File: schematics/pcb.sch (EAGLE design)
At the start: 14 parts

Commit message: Further work on pcb schematics
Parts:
- added C5: 0.33uF, rcl:C-EUC0805
- added C6: 0.1uF, rcl:C-EUC0805
- added CONFIRM, LEFT, RIGHT: CHERRY_MX_LED, cherry:CHERRY_MX_LED
- added IC1: 7805TV, linear:7805TV
- added R6, R7, R8: 1k, rcl:R-EU_R0805
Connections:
- new net N$15: RIGHTG$1.2, UIM.PD6(AIN0/OC0A/PCINT22)
- new net N$16: CONFIRMG$1.2, UIM.PD7(AIN1/PCINT23)
- new net N$18: LEFTLED.A, R6.2
- new net N$19: R7.2, RIGHTLED.A
- new net N$20: CONFIRMLED.A, R8.2
- new net N$9: LEFTG$1.2, UIM.PD5(T1/OC0B/PCINT21)
- new net PWRIN: C5.1, IC1.VI
- net +5V: now also C6.1, IC1.VO, R6.1, R7.1, R8.1
- net GND: now also C5.2, C6.2, CONFIRMG$1.1, CONFIRMLED.C, IC1.GND, LEFTG$1.1, LEFTLED.C, RIGHTG$1.1, RIGHTLED.C
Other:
- moved on the sheet: C3, C4, Q2, R5, TARGET_ISP, UIM

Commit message: Further work on pcb schematics
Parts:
- added BAT: 9V, con-wago-500:W237-102
- added C7, C8: 100nF, rcl:C-EUC0805
- added S1: (no value), Wurth_Switch_WS-SLTV:452404020202
- added U$1: 128X64-I2C-OLED, Parts:128X64-I2C-OLED
- Q1, Q2: value (none) -> 16Mhz
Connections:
- new net N$17: BAT-1.KL, S1.COM1
- new net N$21: C7.1, UIM.AREF
- new net N$22: C8.1, PROGRAMMER.AREF
- net +5V: now also PROGRAMMER.AVCC, U$1.VCC, UIM.AVCC
- net GND: now also BAT-2.KL, C7.2, C8.2, PROGRAMMER.AGND, U$1.GND, UIM.AGND
- net N$1: now also U$1.SCL
- net N$2: now also U$1.SDA
- net PWRIN: now also S1.4
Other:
- note added: "I2C-OLED"
- moved on the sheet: R1, R2, R3

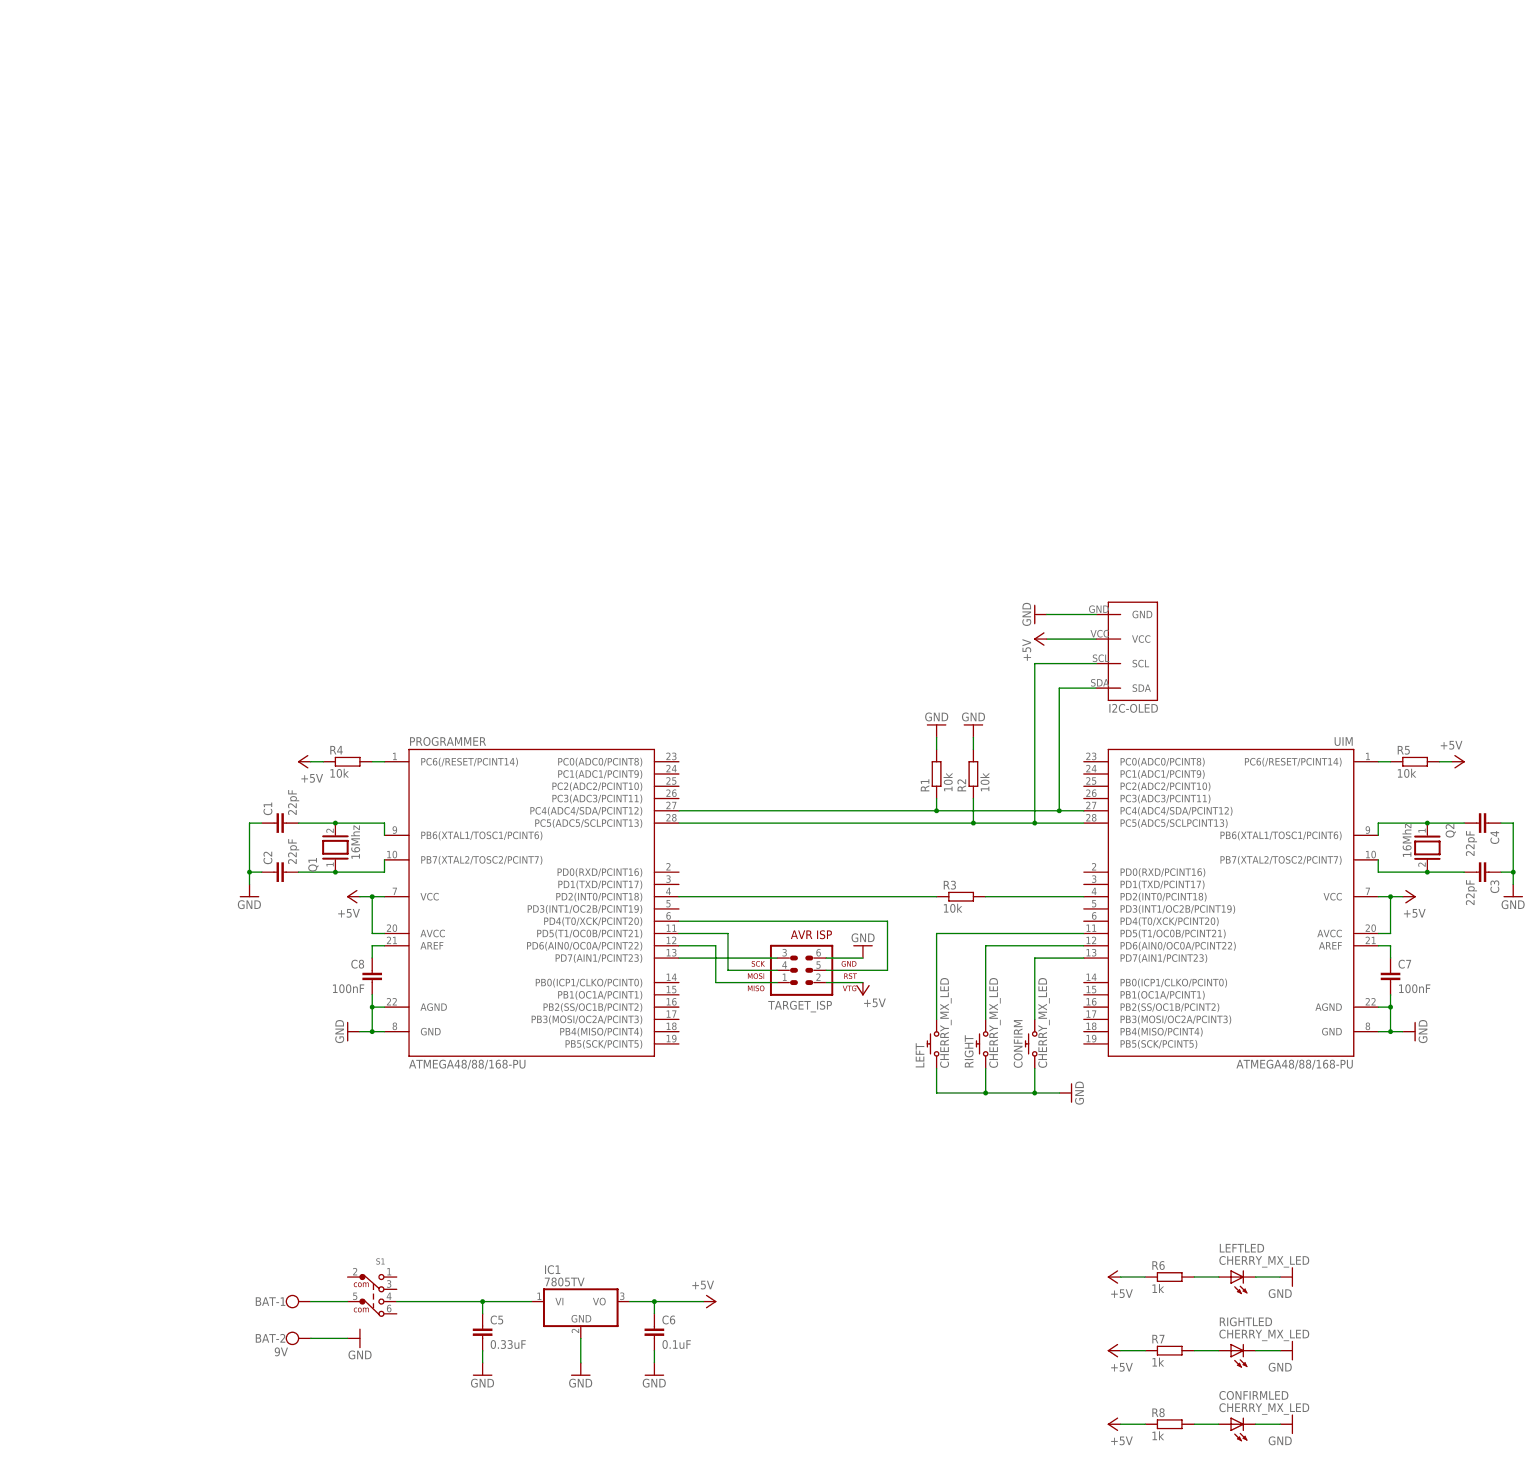
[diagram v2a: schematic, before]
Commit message: Added SD-Card to PCB
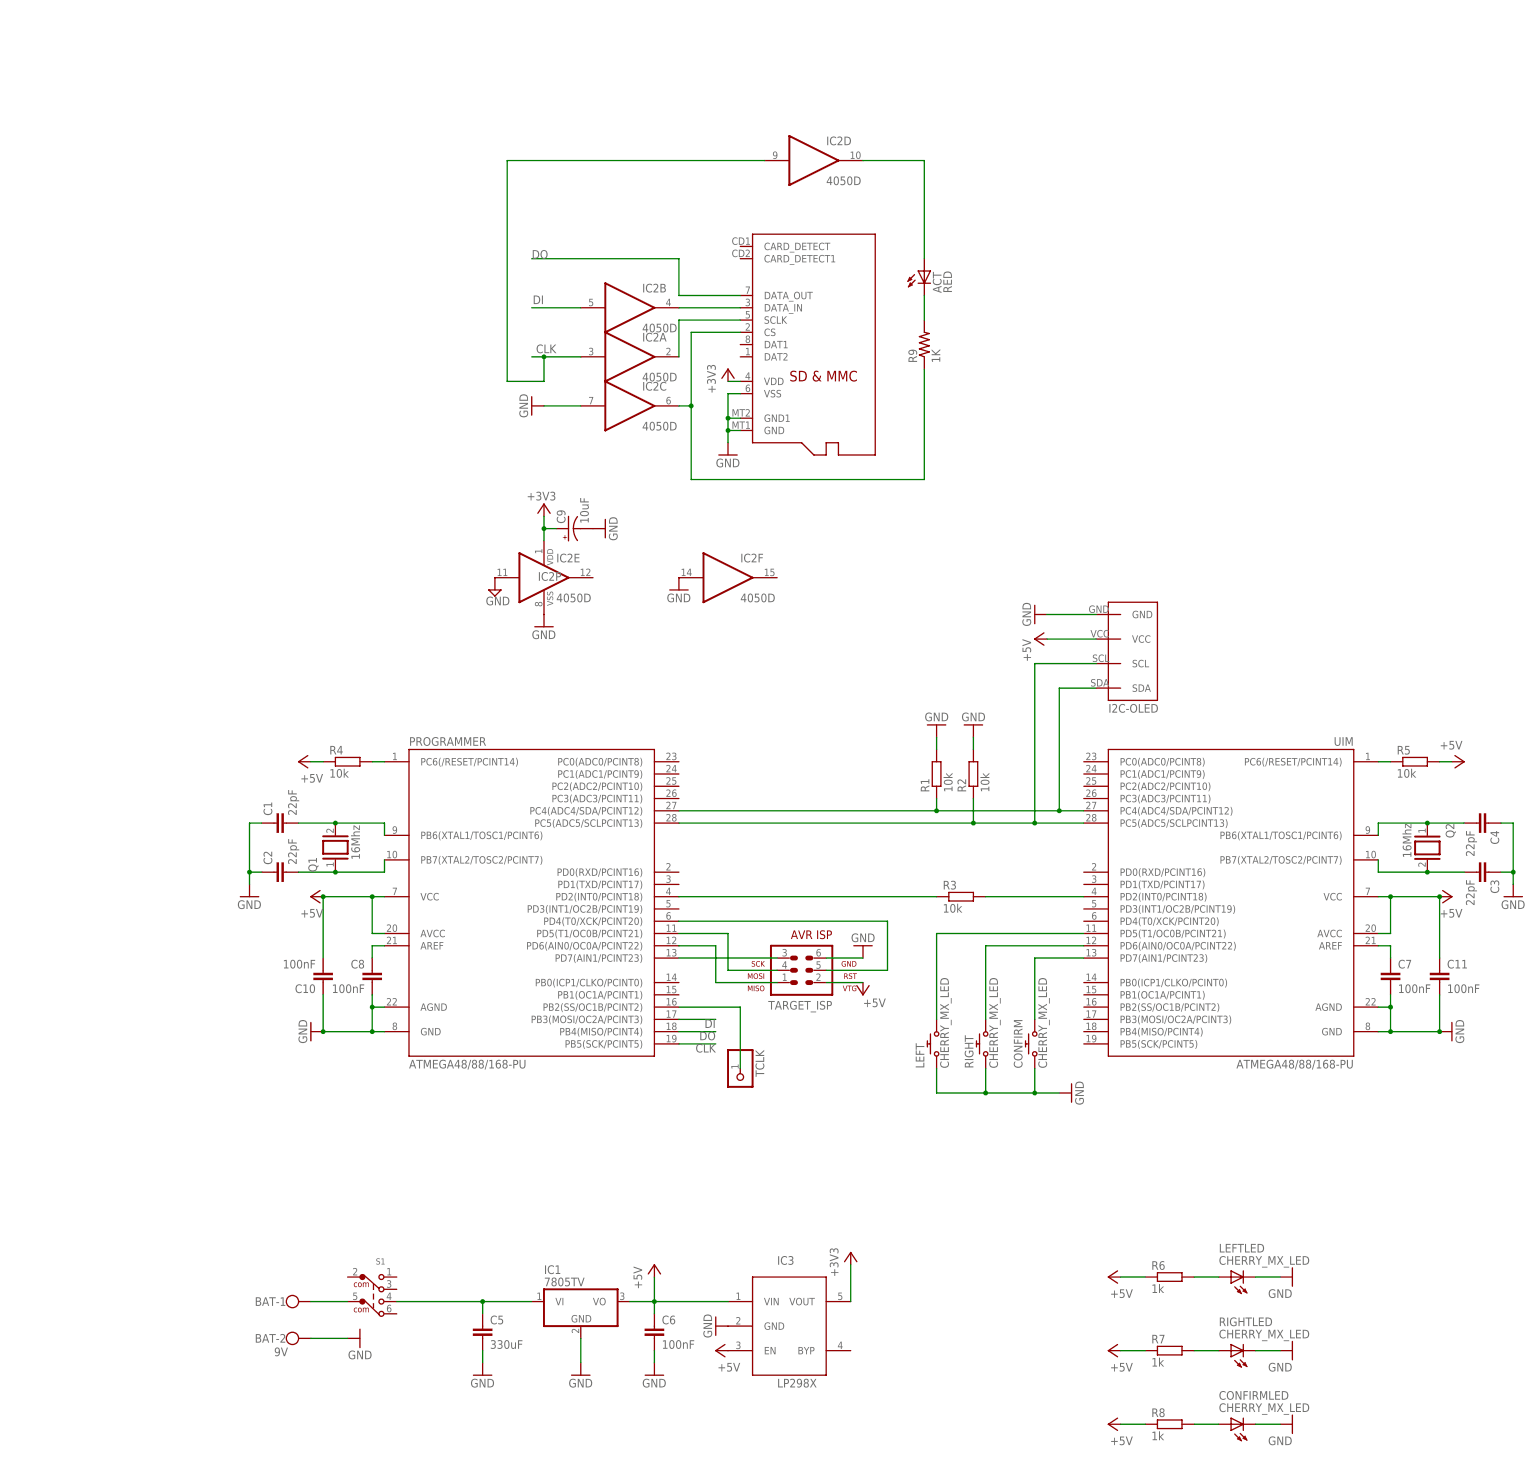
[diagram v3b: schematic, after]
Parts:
- added ACT: RED, adafruit:LEDCHIP-LED0805
- added C10, C11: 100nF, rcl:C-EUC0805
- added C9: 10uF, adafruit:CPOL-USA/3216-18R
- added IC2: 4050D, 40xx:4050D
- added IC3: LP298XS, adafruit:LP298XS
- added R9: 1K, adafruit:R-US_R0805
- added TCLK: (no value), pinhead:PINHD-1X1
- added X1: MICROSD, adafruit:MICROSD
- C5: value 0.33uF -> 330uF
- C6: value 0.1uF -> 100nF
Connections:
- new net +3V3: C9.+, IC2P.VDD, IC3.VOUT, X1.VDD
- new net CLK: IC2A.I, IC2D.I, PROGRAMMER.PB5(SCK/PCINT5)
- new net DI: IC2B.I, PROGRAMMER.PB3(MOSI/OC2A/PCINT3)
- new net DO: PROGRAMMER.PB4(MISO/PCINT4), X1.DATA_OUT
- new net N$23: ACT.A, IC2D.O
- new net N$24: IC2A.O, X1.SCLK
- new net N$25: IC2C.O, R9.1, X1.CS
- new net N$26: ACT.C, R9.2
- new net N$27: IC2B.O, X1.DATA_IN
- new net N$28: PROGRAMMER.PB2(SS/OC1B/PCINT2), TCLK.1
- net +5V: now also C10.2, C11.1, IC3.EN, IC3.VIN
- net GND: now also C10.1, C11.2, C9.-, IC2C.I, IC2E.I, IC2F.I, IC2P.VSS, IC3.GND, X1.GND, X1.GND1, X1.VSS

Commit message: Added Serial debug and reprogramming port to ICs
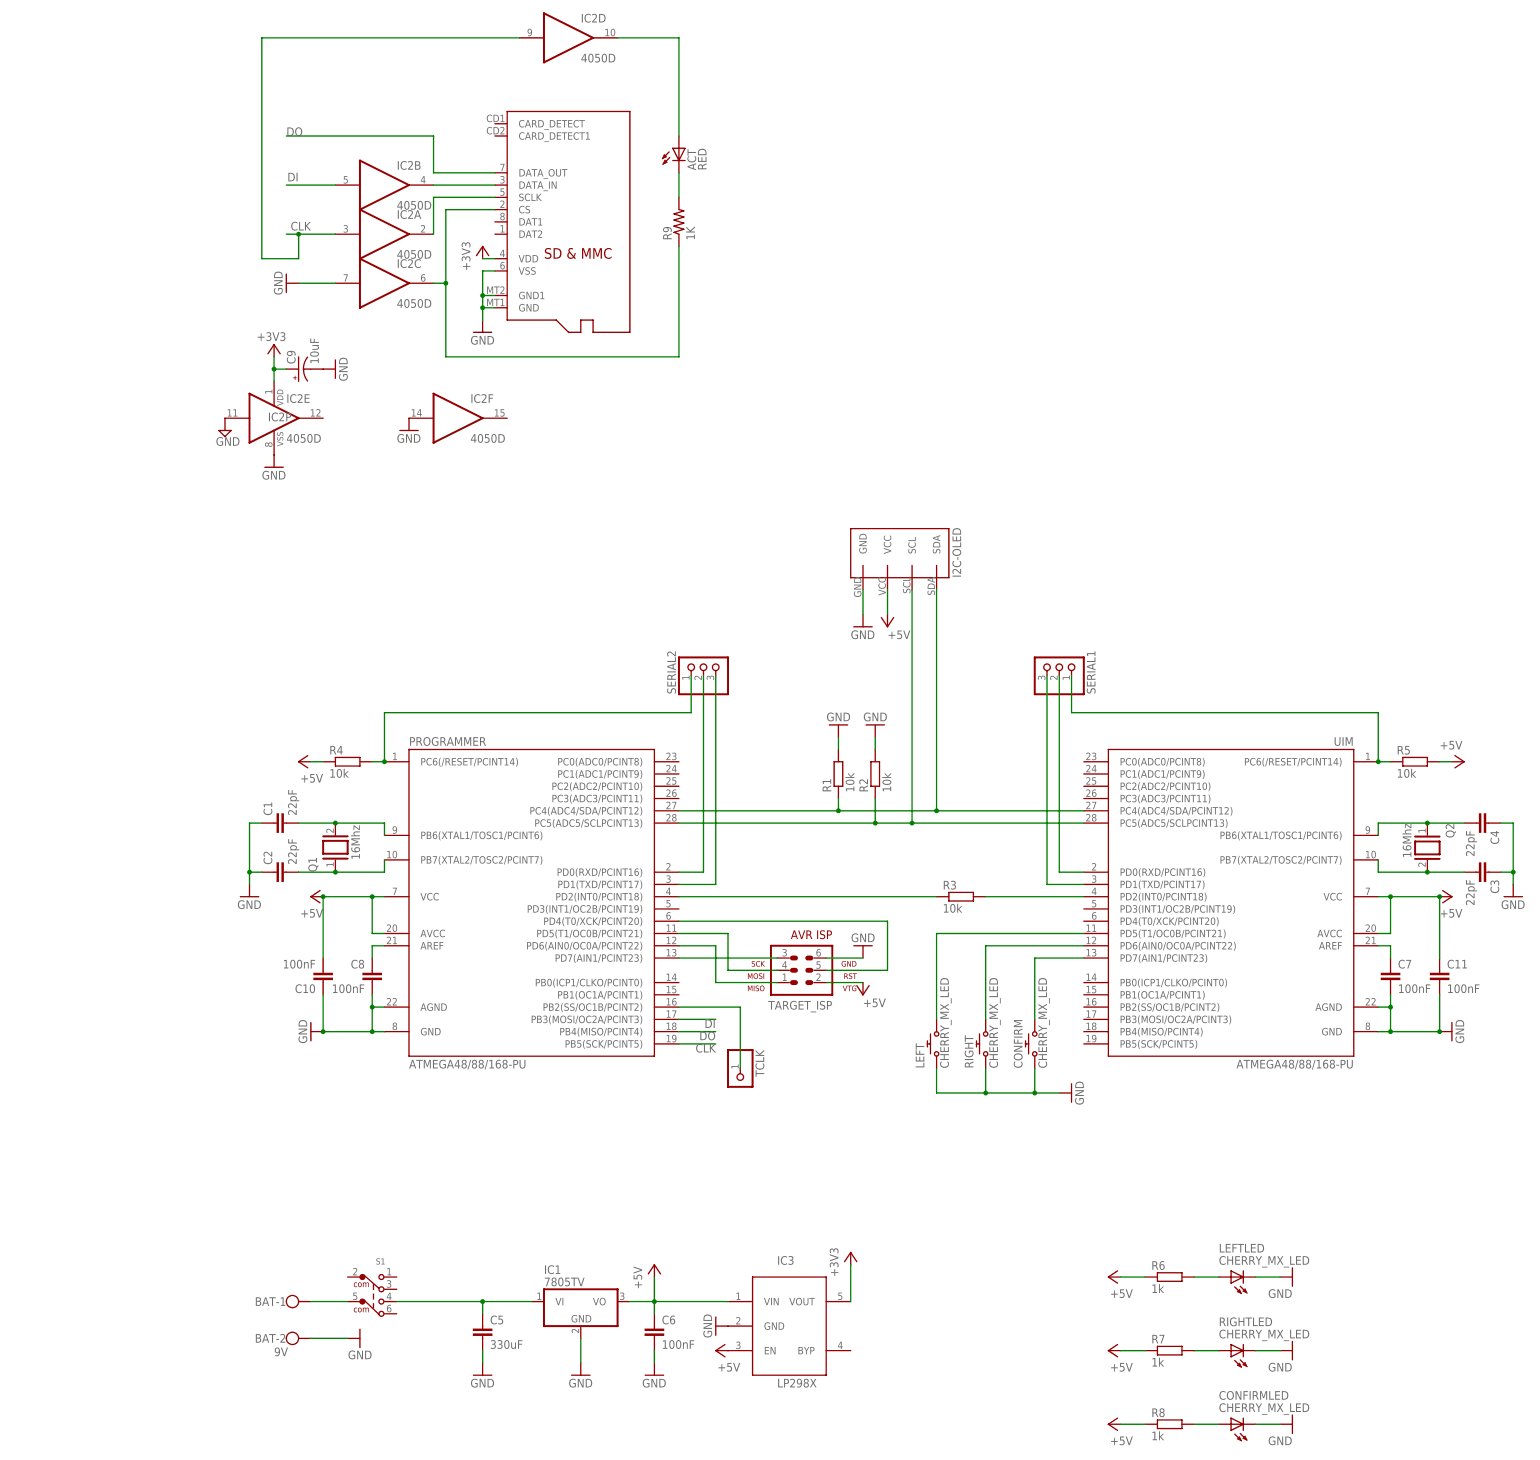
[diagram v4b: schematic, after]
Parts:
- added SERIAL1, SERIAL2: (no value), pinhead:PINHD-1X3
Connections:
- new net N$29: PROGRAMMER.PD0(RXD/PCINT16), SERIAL2.2
- new net N$30: PROGRAMMER.PD1(TXD/PCINT17), SERIAL2.3
- new net N$32: SERIAL1.2, UIM.PD0(RXD/PCINT16)
- new net N$33: SERIAL1.3, UIM.PD1(TXD/PCINT17)
- net N$5: now also SERIAL2.1
- net N$6: now also SERIAL1.1
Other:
- moved on the sheet: ACT, C9, IC2A, IC2B, IC2C, IC2D, IC2E, IC2F, IC2P, R1, R2, R9

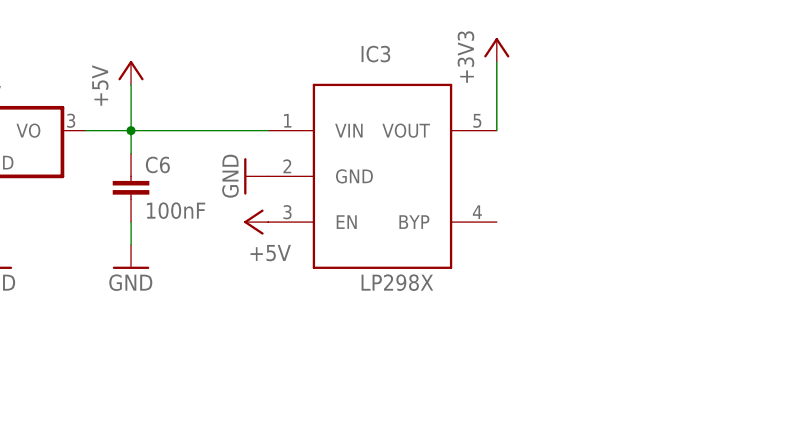
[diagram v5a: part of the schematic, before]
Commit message: Further updates to OLED module
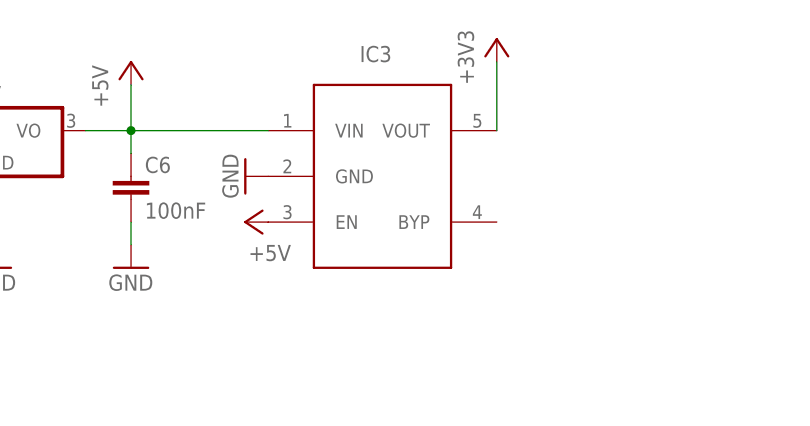
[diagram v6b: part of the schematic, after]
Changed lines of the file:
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@@
 <part name="GND2" library="supply1" library_urn="urn:adsk.eagle:library:371" deviceset="GND" device=""/>
 <part name="P+2" library="supply1" library_urn="urn:adsk.eagle:library:371" deviceset="+5V" device=""/>
-<part name="IC2" library="40xx" deviceset="4050" device="D"/>
-<part name="X1" library="adafruit" deviceset="MICROSD" device=""/>
+<part name="IC2" library="40xx" library_urn="urn:adsk.eagle:library:80" deviceset="4050" device="D" package3d_urn="urn:adsk.eagle:package:821/2"/>
+<part name="X1" library="adafruit" library_urn="urn:adsk.eagle:library:420" deviceset="MICROSD" device="" package3d_urn="urn:adsk.eagle:package:6240723/1"/>
 <part name="+3V1" library="supply1" deviceset="+3V3" device=""/>
 <part name="+3V2" library="supply1" deviceset="+3V3" device=""/>
 <part name="+3V3" library="supply1" deviceset="+3V3" device=""/>
-<part name="IC3" library="adafruit" deviceset="LP298X" device="S"/>
-<part name="C9" library="adafruit" deviceset="CPOL-US" device="A/3216-18R" value="10uF"/>
-<part name="SUPPLY8" library="supply2" deviceset="GND" device=""/>
-<part name="ACT" library="adafruit" deviceset="LED" device="CHIP-LED0805" value="RED"/>
-<part name="R9" library="adafruit" deviceset="R-US_" device="R0805" value="1K"/>
+<part name="IC3" library="adafruit" library_urn="urn:adsk.eagle:library:420" deviceset="LP298X" device="S" package3d_urn="urn:adsk.eagle:package:6240724/1"/>
+<part name="C9" library="adafruit" library_urn="urn:adsk.eagle:library:420" deviceset="CPOL-US" device="A/3216-18R" package3d_urn="urn:adsk.eagle:package:6240466/1" value="10uF"/>
+<part name="SUPPLY8" library="supply2" library_urn="urn:adsk.eagle:library:372" deviceset="GND" device=""/>
+<part name="ACT" library="adafruit" library_urn="urn:adsk.eagle:library:420" deviceset="LED" device="CHIP-LED0805" package3d_urn="urn:adsk.eagle:package:6240557/1" value="RED"/>
+<part name="R9" library="adafruit" library_urn="urn:adsk.eagle:library:420" deviceset="R-US_" device="R0805" package3d_urn="urn:adsk.eagle:package:6240566/1" value="1K"/>
 <part name="P+11" library="supply1" library_urn="urn:adsk.eagle:library:371" deviceset="+5V" device=""/>
 <part name="P+12" library="supply1" library_urn="urn:adsk.eagle:library:371" deviceset="+5V" device=""/>
